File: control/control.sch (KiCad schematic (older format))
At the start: 4 parts, among them J1 CONTROL

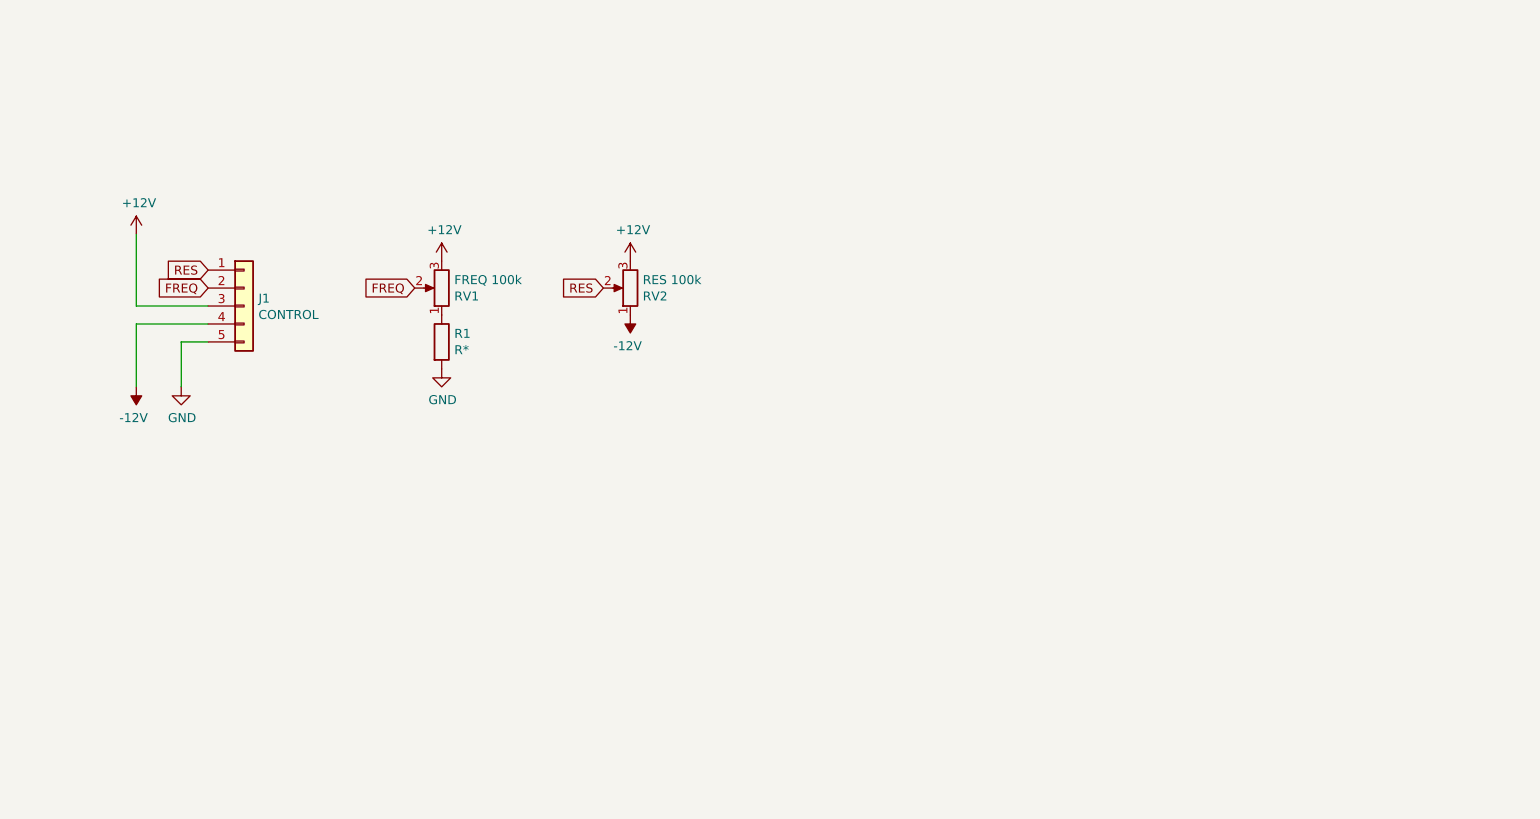
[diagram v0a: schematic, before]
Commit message: Update control board
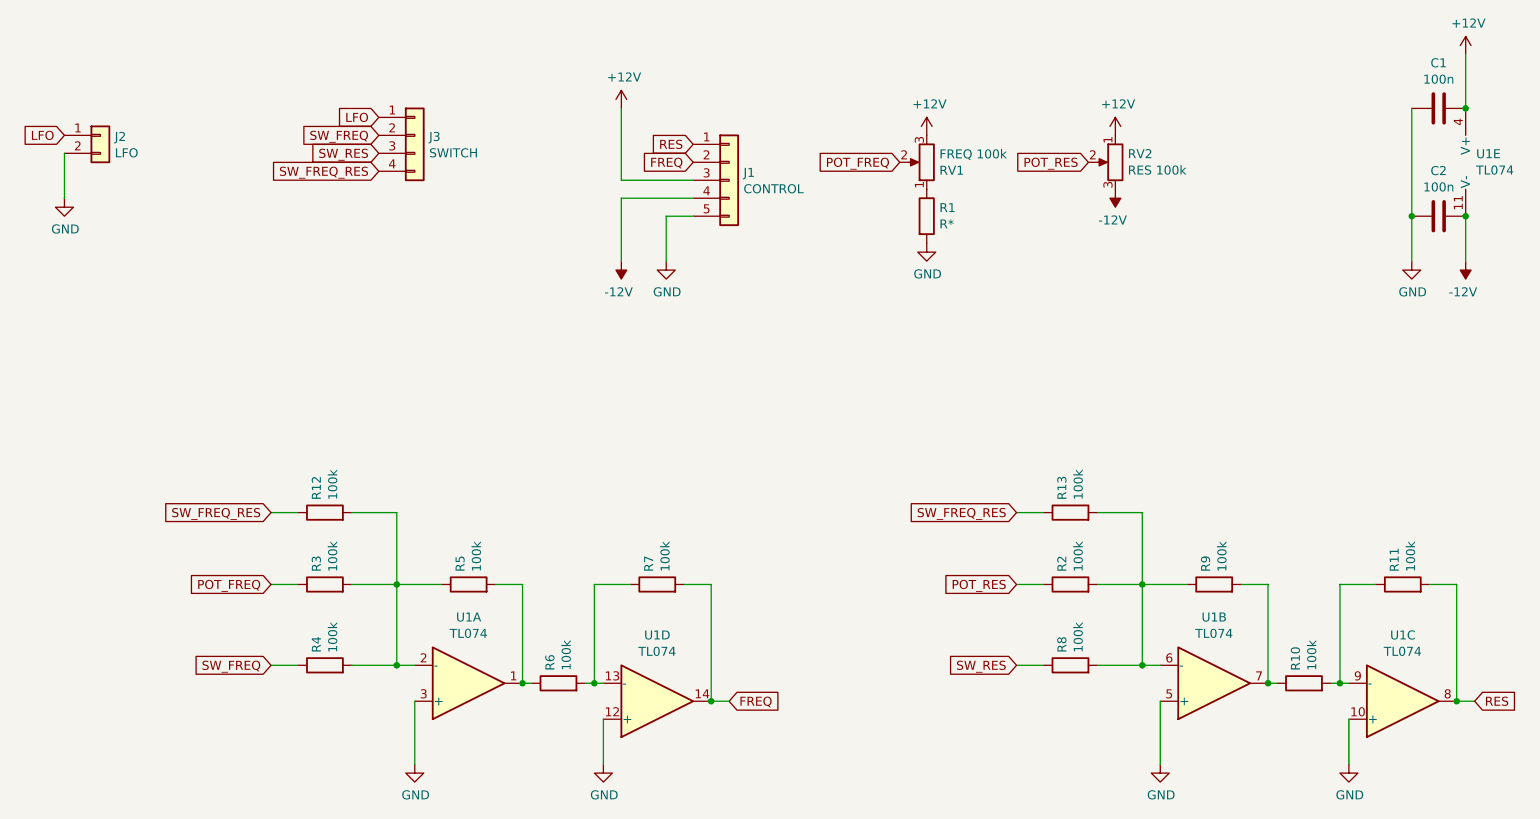
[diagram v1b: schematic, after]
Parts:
- added C1, C2: 100n, Capacitor_THT:C_Disc_D3.0mm_W2.0mm_P2.50mm, symbol Device:C
- added J2: LFO, Connector_Molex:Molex_KK-254_AE-6410-02A_1x02_P2.54mm_Vertical, symbol Connector_Generic:Conn_01x02
- added J3: SWITCH, Connector_Molex:Molex_KK-254_AE-6410-04A_1x04_P2.54mm_Vertical, symbol Connector_Generic:Conn_01x04
- added R10, R11, R12, R13, R2, R3, R4, R5, R6, R7, R8, R9: 100k, Resistor_THT:R_Axial_DIN0207_L6.3mm_D2.5mm_P10.16mm_Horizontal, symbol Device:R
- added U1: TL074, Package_DIP:DIP-14_W7.62mm_Socket_LongPads, symbol Amplifier_Operational:TL074
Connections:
- net +12V: now also RV2.1, C1.2, U1.4 (V+); no longer RV2.3
- net -12V: now also RV2.3, C2.2, U1.11 (V-); no longer RV2.1
- net FREQ: now also R7.2, U1.14; no longer RV1.2
- net GND: now also C1.1, C2.1, J2.2 (Pin_2), U1.10 (+), U1.12 (+), U1.3 (+), U1.5 (+)
- net RES: now also R11.2, U1.8; no longer RV2.2
- new net: R12.2, R3.2, R4.2, R5.1, U1.2 (-)
- new net: R5.2, R6.1, U1.1
- new net: R6.2, R7.1, U1.13 (-)
- new net: R10.2, R11.1, U1.9 (-)
- new net: R13.2, R2.2, R8.2, R9.1, U1.6 (-)
- new net: R10.1, R9.2, U1.7
- new net LFO: J2.1 (Pin_1), J3.1 (Pin_1)
- new net POT_FREQ: R3.1, RV1.2
- new net POT_RES: R2.1, RV2.2
- new net SW_FREQ: J3.2 (Pin_2), R4.1
- new net SW_FREQ_RES: J3.4 (Pin_4), R12.1, R13.1
- new net SW_RES: J3.3 (Pin_3), R8.1
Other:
- moved on the sheet: J1, R1, RV1, RV2
